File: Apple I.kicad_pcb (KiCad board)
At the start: 4 copper layers, 55 parts, among them J1 PS/2 Keyboard, J4 Processor Bus Connector, SW1 Reset, SW2 Video Reset, U1 W65C02SxP, U10 ATmega328P-P, U11 2.8 TFT SPI 240x320 V1.2, U12 SN74AHC125N, U2 UT62256CPCL, U3 W27C512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

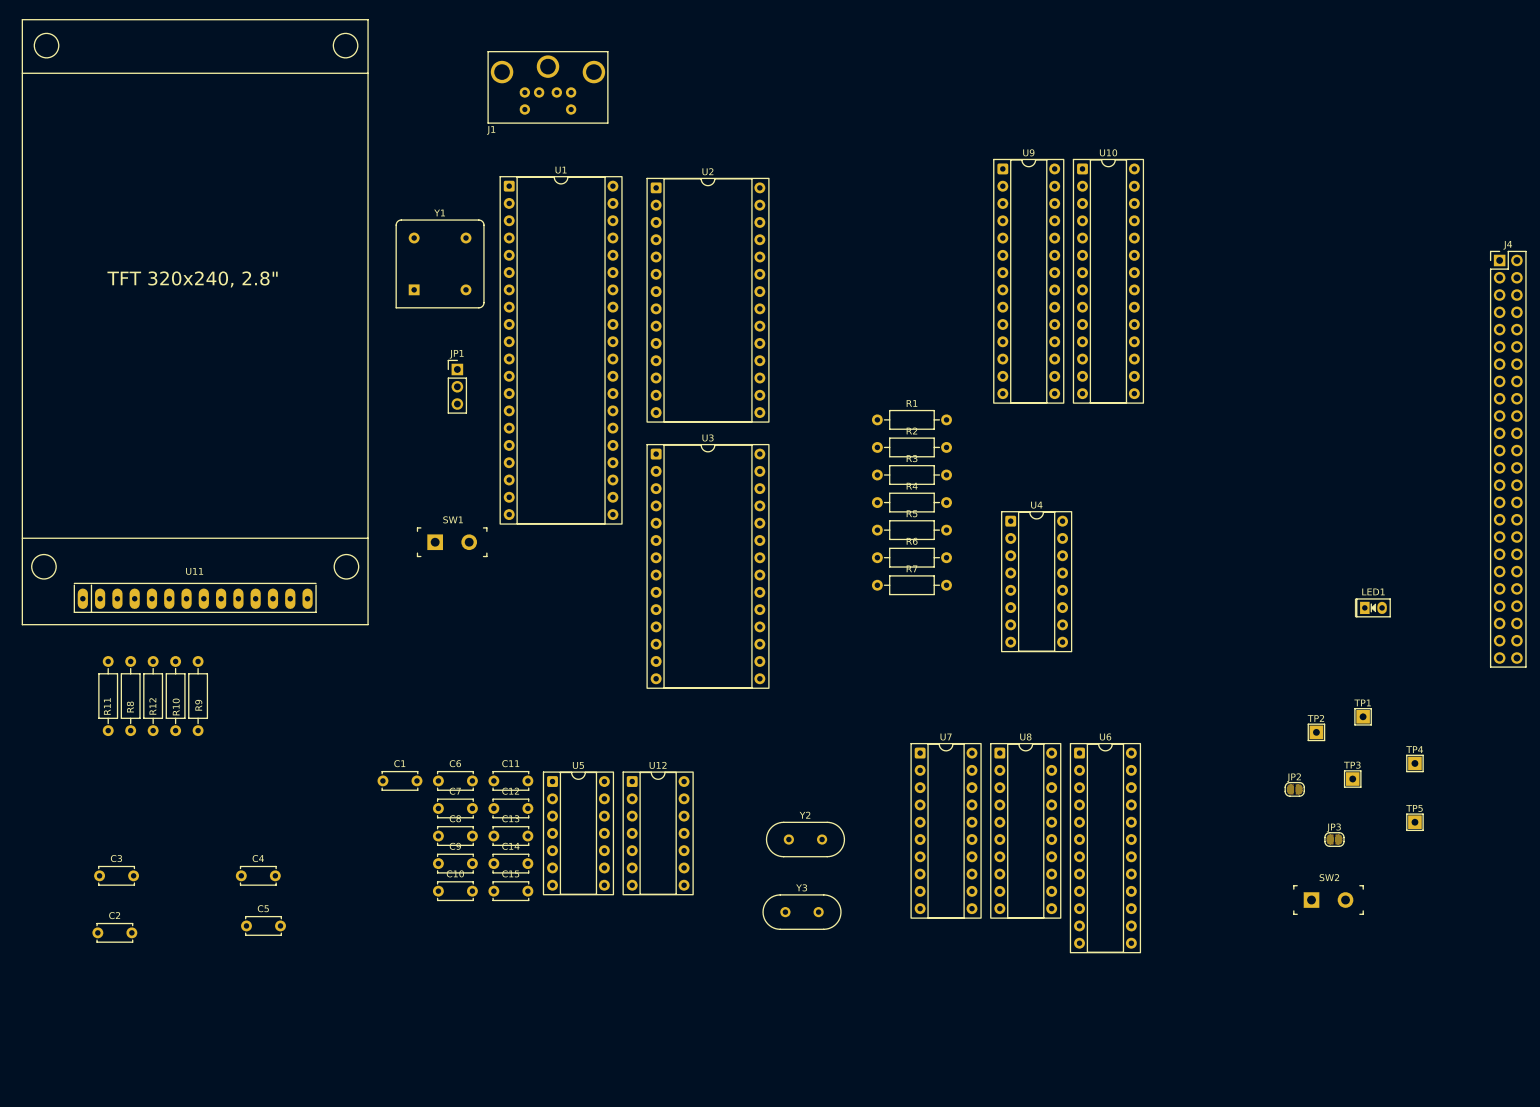
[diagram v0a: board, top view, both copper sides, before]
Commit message: Additional pcb layout
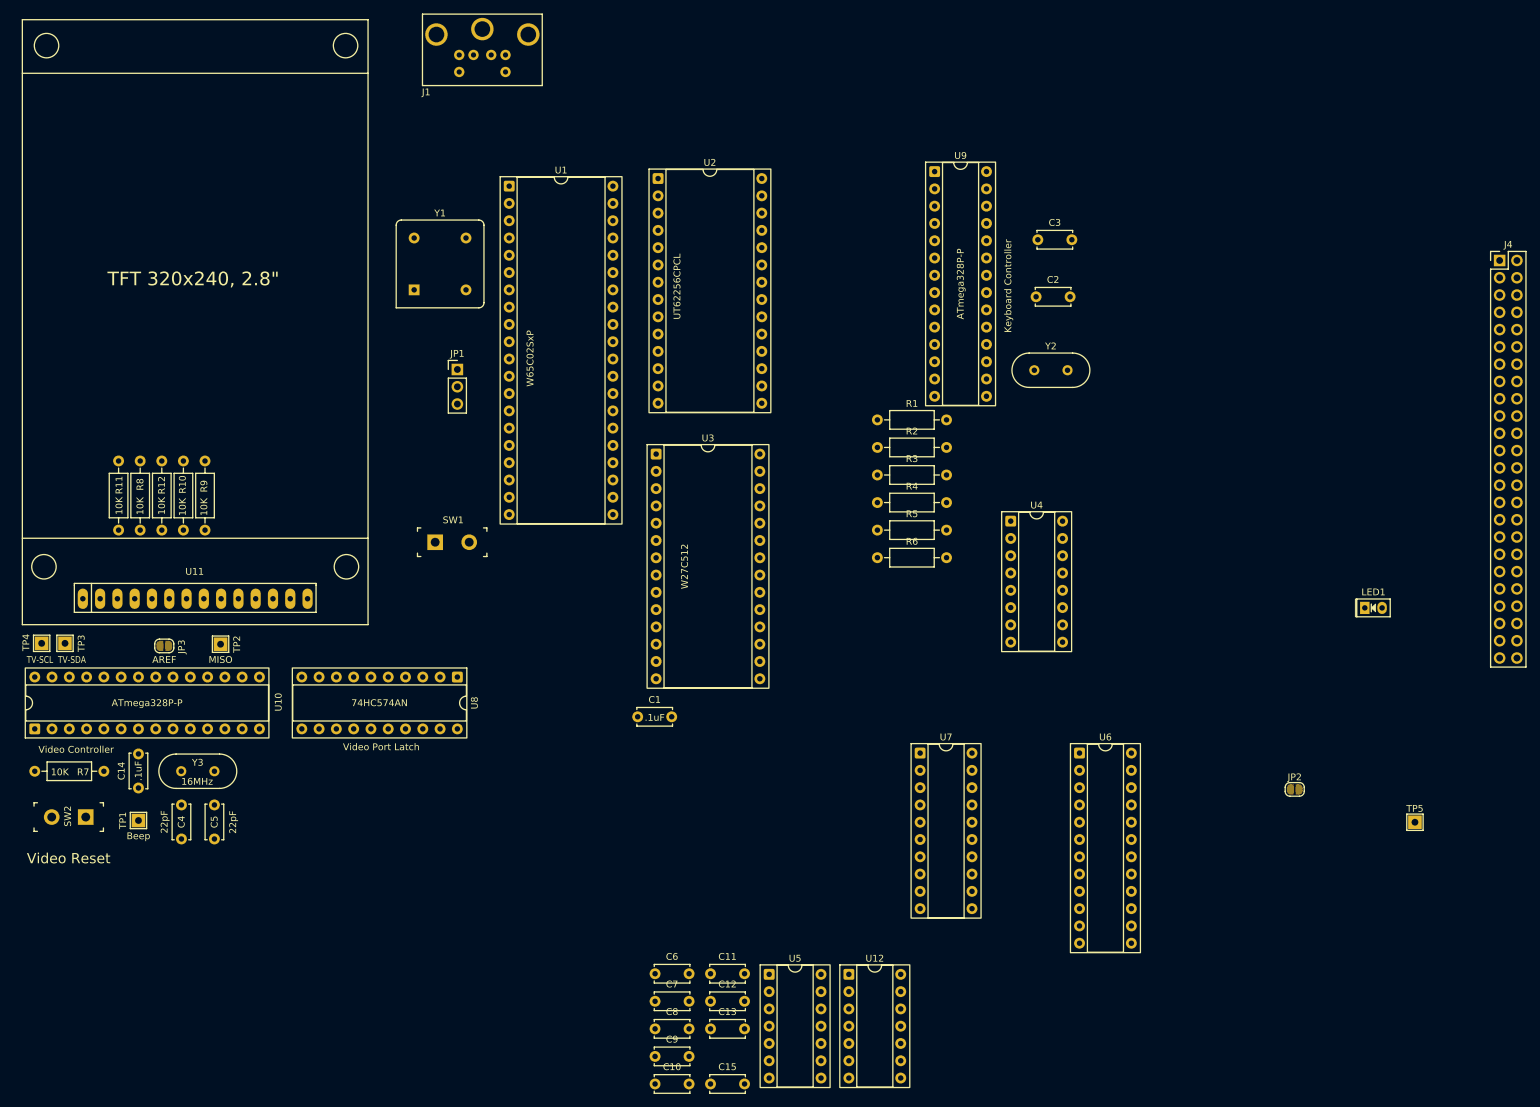
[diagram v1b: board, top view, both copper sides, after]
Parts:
- moved TP4 202.6 mm to (42.8, 109.1)
- moved TP3 190.3 mm to (46.2, 109.1)
- moved TP1 180.6 mm to (57.0, 135.1)
- moved SW2 180.5 mm to (49.3, 134.6), turned to 180 degrees
- moved U10 174.6 mm to (41.8, 121.7), turned to 90 degrees
- moved JP3 174.3 mm to (60.8, 109.5)
- moved C2 166.6 mm to (188.9, 58.2)
- moved C3 166.6 mm to (189.2, 49.8)
- moved TP2 161.6 mm to (69.1, 109.2)
- moved R7 126.8 mm to (41.8, 127.9)
- moved Y3 86.4 mm to (68.2, 127.9), turned to 180 degrees
- moved U8 80.5 mm to (103.9, 114.0), turned to -90 degrees
- moved Y2 77.8 mm to (188.7, 69.0)
- moved C14 53.4 mm to (57.0, 130.3), turned to 90 degrees
- moved C10 42.6 mm to (132.9, 173.8)
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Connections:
- J1 pad 7: (no net) -> GND

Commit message: More work on PCB Placement and routing
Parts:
- added D1: LTA-1000G, digikey-footprints:LED_Bar_Graph_LTA-1000, F.Cu at (206.5, 54.0)
- added D2: LTA-1000G, digikey-footprints:LED_Bar_Graph_LTA-1000, F.Cu at (206.5, 82.9)
- added H1: Corner, MountingHole:MountingHole_3.2mm_M3, F.Cu at (60.7, 28.7)
- added H2: Corner, MountingHole:MountingHole_3.2mm_M3, F.Cu at (60.7, 154.2)
- added H3: Corner, MountingHole:MountingHole_3.2mm_M3, F.Cu at (228.3, 28.7)
- added H4: Corner, MountingHole:MountingHole_3.2mm_M3, F.Cu at (228.3, 154.2)
- added H5: Display, MountingHole:MountingHole_3.2mm_M3, F.Cu at (67.2, 34.9)
- added H6: Display, MountingHole:MountingHole_3.2mm_M3, F.Cu at (111.1, 34.9)
- added H7: Display, MountingHole:MountingHole_3.2mm_M3, F.Cu at (111.3, 111.5)
- added H8: Display, MountingHole:MountingHole_3.2mm_M3, F.Cu at (66.8, 111.5)
- added J2: Power Terminal, TerminalBlock_Phoenix:TerminalBlock_Phoenix_PT-1,5-2-5.0-H_1x02_P5.00mm_Horizontal, F.Cu at (158.2, 34.8)
- added JP4: ~{LED En}, Jumper:SolderJumper-2_P1.3mm_Open_RoundedPad1.0x1.5mm, F.Cu at (211.1, 55.3)
- added JP5: LED En, Jumper:SolderJumper-2_P1.3mm_Open_RoundedPad1.0x1.5mm, F.Cu at (194.8, 46.5)
- added JP6: ~{LED En}, Jumper:SolderJumper-2_P1.3mm_Open_RoundedPad1.0x1.5mm, F.Cu at (211.1, 89.2)
- added RN1: 1K, Resistor_THT:R_Array_SIP9, F.Cu at (211.1, 51.4)
- added RN2: 2K, Resistor_THT:R_Array_SIP5, F.Cu at (194.8, 50.4)
- added RN3: 1K, Resistor_THT:R_Array_SIP9, F.Cu at (211.1, 85.5)
- added TP6: LED, TestPoint:TestPoint_THTPad_2.0x2.0mm_Drill1.0mm, F.Cu at (216.0, 51.6)
- added TP7: LED, TestPoint:TestPoint_THTPad_2.0x2.0mm_Drill1.0mm, F.Cu at (216.0, 55.1)
- added TP8: ~{LED}, TestPoint:TestPoint_THTPad_2.0x2.0mm_Drill1.0mm, F.Cu at (216.0, 72.6)
- J4: footprint Connector_PinHeader_2.54mm:PinHeader_2x24_P2.54mm_Vertical -> Connector_PinHeader_2.54mm:PinHeader_2x24_P2.54mm_Vertical_Counter_Clockwise
- moved TP5 145.4 mm to (122.2, 57.0)
- moved C11 134.0 mm to (183.5, 30.5), turned to 180 degrees
- moved LED1 133.0 mm to (122.2, 37.2), turned to -90 degrees
- moved JP2 119.6 mm to (146.8, 41.7)
- moved C10 104.6 mm to (197.6, 91.7), turned to -90 degrees
- moved C13 104.1 mm to (142.2, 61.6), turned to 90 degrees
- moved C6 102.0 mm to (168.2, 61.9)
- moved Y1 101.3 mm to (153.5, 141.6), turned to -90 degrees
- moved U1 99.8 mm to (154.8, 131.8), turned to 180 degrees
- moved J4 98.8 mm to (225.8, 146.6), turned to 180 degrees
- moved C8 96.8 mm to (208.0, 104.6)
- moved U5 95.1 mm to (122.2, 66.7)
- moved U7 94.8 mm to (167.6, 30.6)
- moved JP1 81.4 mm to (145.8, 138.7), turned to -90 degrees
- moved U2 78.7 mm to (174.6, 107.9)
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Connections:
- J1 pad 4: +5V -> Net-(J1-Pad4)
- R5 pad 2: +5V -> Net-(J1-Pad4)
- R6 pad 2: +5V -> GND
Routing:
- net KBIT7: track 0.00 -> 81.2 mm
- net /D7: track 0.00 -> 64.9 mm
- net /SPI.SCK: track 0.00 -> 56.6 mm
- net VBIT7: track 0.00 -> 53.6 mm
- net /SPI.MOSI: track 0.00 -> 49.9 mm
- net /SPI.DC: track 0.00 -> 44.1 mm
- net /D6: track 0.00 -> 41.8 mm
- net /D5: track 0.00 -> 38.3 mm
- net /VD0: track 0.00 -> 36.7 mm
- net /D4: track 0.00 -> 34.7 mm
- net /SPI.RST: track 0.00 -> 33.1 mm
- net ~{Video}: track 0.00 -> 31.8 mm
- net /D3: track 0.00 -> 31.1 mm
- net /VD1: track 0.00 -> 29.8 mm
- net /D2: track 0.00 -> 27.4 mm
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- added copper zone on In2.Cu, net +5V
- added copper zone on In1.Cu, net GND
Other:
- board outline added: 175 x 133 mm
- board text added: "$~{8xxx}"
- board text added: "$~{9xxx}"
- board text added: "$~{Axxx}"
- board text added: "$~{Bxxx}"
- board text added: "$~{Cxxx}"
- board text added: "$~{Dxxx}"
- board text added: "$~{Exxx}"
- board text added: "$~{Fxxx}"
- board text added: "+5V"
- board text added: "A0"
- board text added: "A1"
- board text added: "A10"
- board text added: "A11"
- board text added: "A12"
- board text added: "A13"
- board text added: "A14"
- board text added: "A15"
- board text added: "A2"
- board text added: "A3"
- board text added: "A4"
- board text added: "A5"
- board text added: "A6"
- board text added: "A7"
- board text added: "A8"
- board text added: "A9"
- board text added: "Clk In"
- board text added: "D0"
- board text added: "D1"
- board text added: "D2"
- board text added: "D3"
- board text added: "D4"
- board text added: "D5"
- board text added: "D6"
- board text added: "D7"
- board text added: "Expansion"
- board text added: "GND"
- board text added: "PIA"
- board text added: "Phi1"
- board text added: "Phi2"
- board text added: "ROM"
- board text added: "~{IRQ}"
- board text added: "~{Kbd_Bit7}"
- board text added: "~{Keyboard}"
- board text added: "~{NMI}"
- board text added: "~{ROM_SEL}"
- board text added: "~{R}"
- board text added: "~{Vid_Bit7}"
- board text added: "~{Video}"
- board text added: "~{W}"

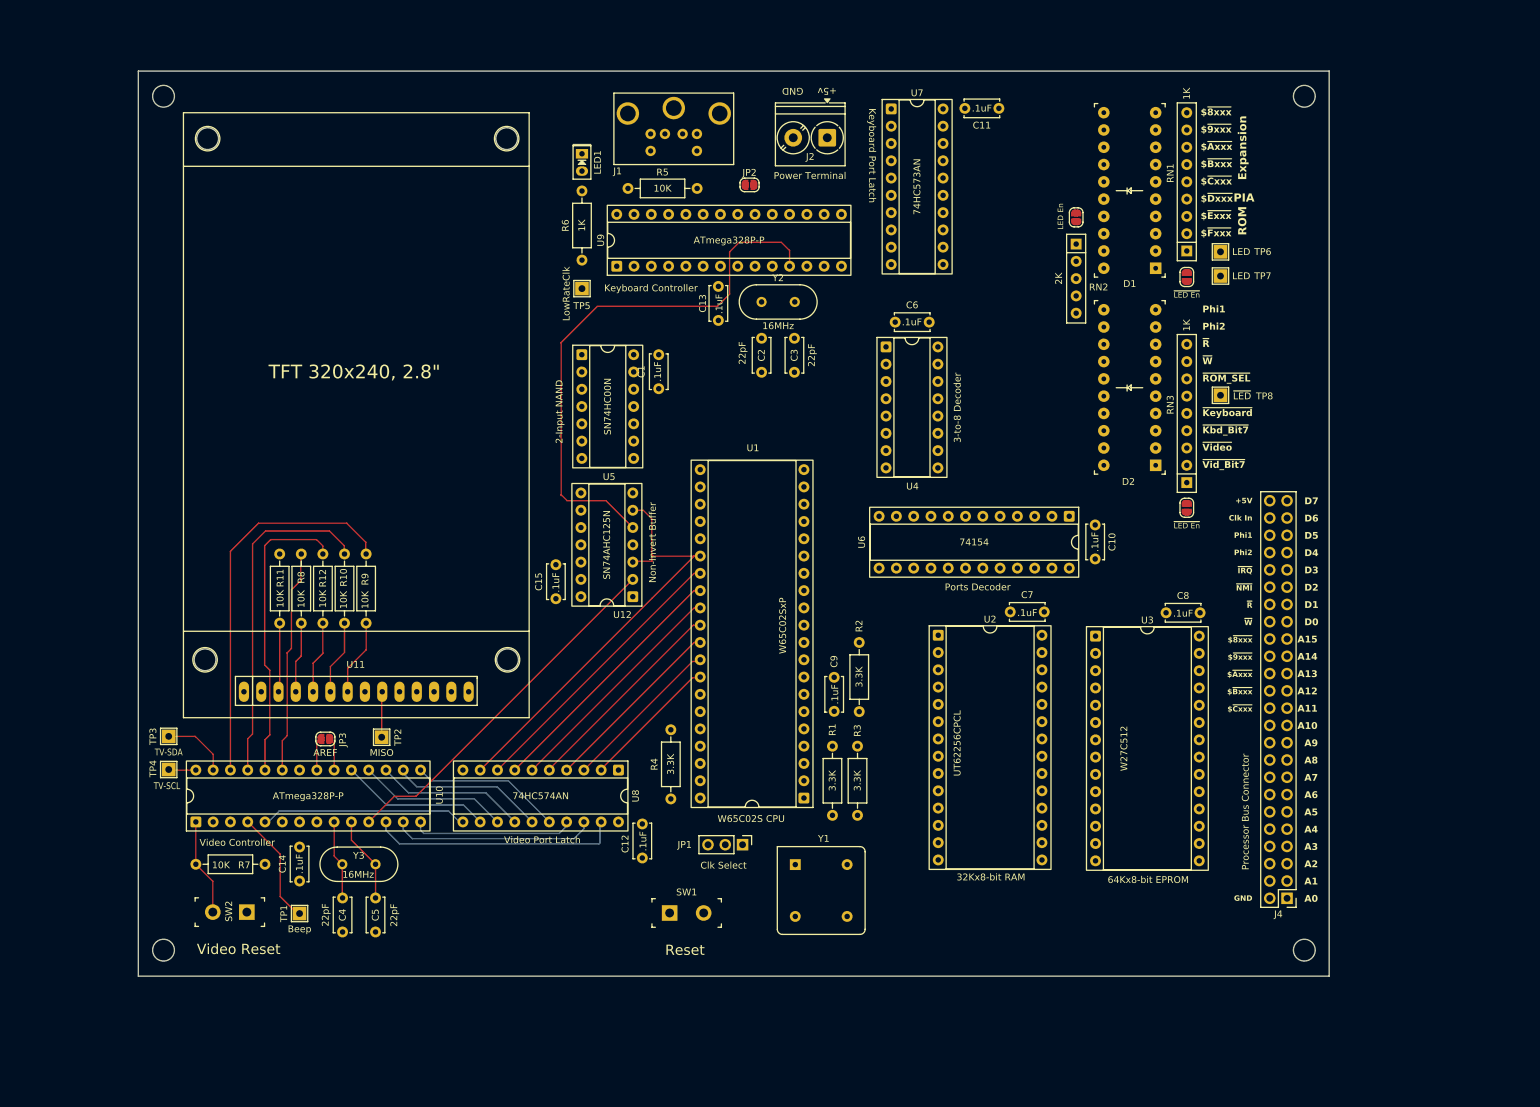
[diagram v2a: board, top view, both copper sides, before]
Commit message: First pass routing finished
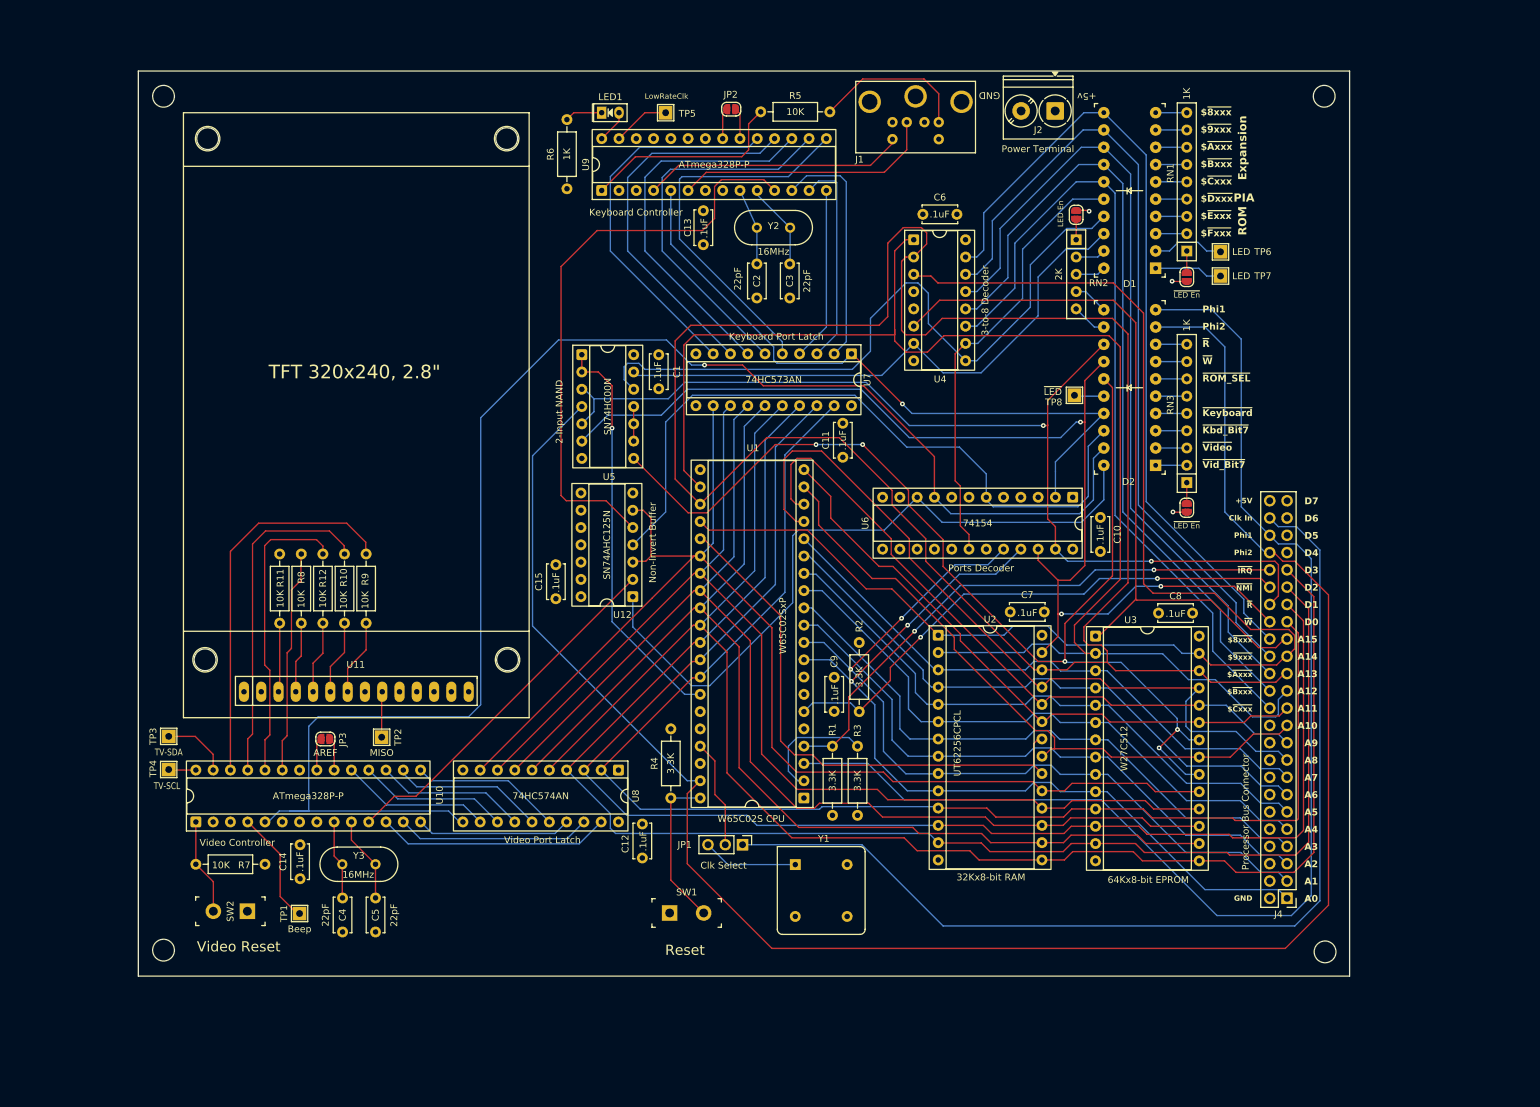
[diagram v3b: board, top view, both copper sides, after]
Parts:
- moved C11 56.2 mm to (160.5, 81.7), turned to 90 degrees
- moved U7 36.5 mm to (161.8, 66.5), turned to -90 degrees
- moved J1 35.6 mm to (171.2, 24.0)
- moved J2 33.7 mm to (191.7, 30.9)
- moved TP5 28.6 mm to (134.5, 31.1), turned to 180 degrees
- moved R5 22.5 mm to (148.5, 31.0)
- moved TP8 21.5 mm to (194.6, 72.6)
- moved C6 16.4 mm to (172.3, 46.0)
- moved U4 16.3 mm to (170.9, 49.8)
- moved JP2 11.5 mm to (144.1, 30.6)
- moved C13 11.3 mm to (140.0, 50.5)
- moved U9 11.3 mm to (125.1, 42.5)
- moved C2 10.9 mm to (147.9, 53.3)
- moved C3 10.9 mm to (152.7, 53.3)
- moved Y2 10.9 mm to (147.9, 48.0)
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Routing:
- net /A13: track 0.00 -> 291.3 mm
- net Phi2: track 0.00 -> 285.8 mm
- net /A12: track 0.00 -> 215.4 mm
- net /A15: track 0.00 -> 210.5 mm
- net ~{Video}: track 31.8 -> 233.7 mm, vias 0 -> 1
- net /A14: track 0.00 -> 201.5 mm
- net /D3: track 31.1 -> 229.3 mm
- net /D2: track 27.4 -> 224.3 mm
- net /D1: track 23.8 -> 213.9 mm
- net Phi1: track 0.00 -> 187.0 mm
- net /D0: track 20.3 -> 204.9 mm
- net /D4: track 34.7 -> 217.0 mm
- net /D5: track 38.3 -> 217.6 mm
- net /D6: track 41.8 -> 216.8 mm
- net /D7: track 64.9 -> 235.7 mm
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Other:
- board size 175 x 133 mm -> 178 x 133 mm
